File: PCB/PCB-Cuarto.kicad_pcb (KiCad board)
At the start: 4 copper layers, 90 x 100 mm, 80 parts, among them IC100 AP63203WU-7, J100 2604-3102, J200 2171790001, J201 2086-1104, J300 2086-1102, J301 jumper, J302 2086-1104, J303 2086-1104, Q100 CSD19537Q3, Q101 BSS138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

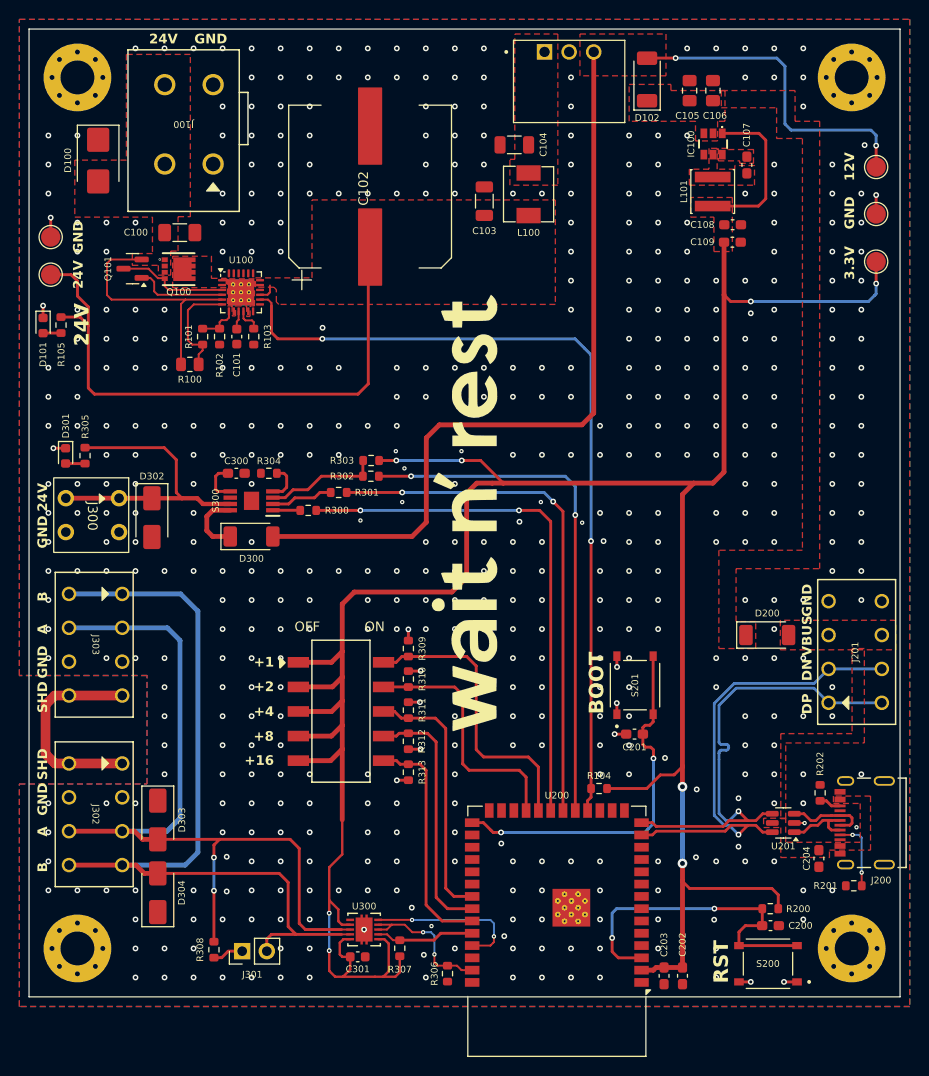
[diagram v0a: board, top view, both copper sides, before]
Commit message: Mejora en ruteo
- Se ha mejorado el ruteo de potencia
- Se ha generado los files para JLCPCB
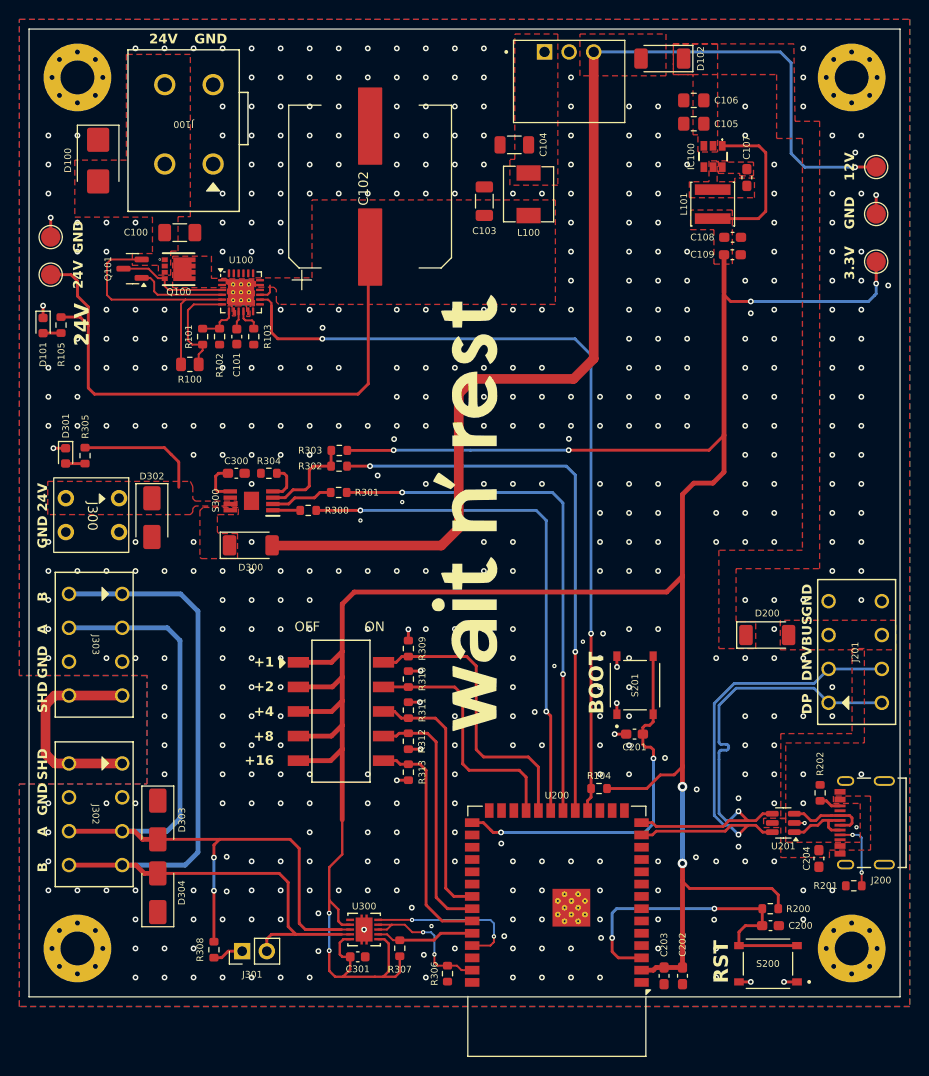
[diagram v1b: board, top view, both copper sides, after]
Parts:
- moved R302 3.45 mm to (137.0, 93.2)
- moved R303 3.45 mm to (137.1, 91.5)
- moved C105 3.45 mm to (173.7, 57.8), turned to 180 degrees
- moved D102 2.67 mm to (170.4, 51.1), turned to 180 degrees
- moved C106 2.22 mm to (173.7, 55.4), turned to 180 degrees
- moved C108 1.30 mm to (177.7, 69.5)
- moved C109 1.30 mm to (177.7, 71.3)
- moved L101 1.30 mm to (175.6, 66.1)
- moved C107 1.30 mm to (179.2, 63.3)
- moved IC100 1.30 mm to (175.7, 61.2)
- moved D300 0.92 mm to (127.9, 101.3)
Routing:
- net Net-(D302-A1): track 31.4 -> 12.9 mm
- net +3.3V: track 287.2 -> 301.4 mm
- net Net-(D300-K): track 6.83 -> 0.00 mm
- net +12V: track 114.6 -> 120.7 mm, vias 2 -> 1
- net /MCU/DOOR_FAULT: track 54.2 -> 58.6 mm
- net Net-(S300-~{FAULT}): track 11.9 -> 9.97 mm
- net /MCU/DOOR_DIAG_EN: track 54.1 -> 54.6 mm
- net GND: vias 520 -> 489
- added copper zone on F.Cu, net Net-(D300-K)
- added copper zone on F.Cu, net Net-(D302-A1)

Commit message: Cambio de footprint del eFuse
- Se cambio el footprint del eFuse debido a que el actual no hay stock en JLCPCB
- Se creo de nuevo los archivos de configuracion de JLCPCB
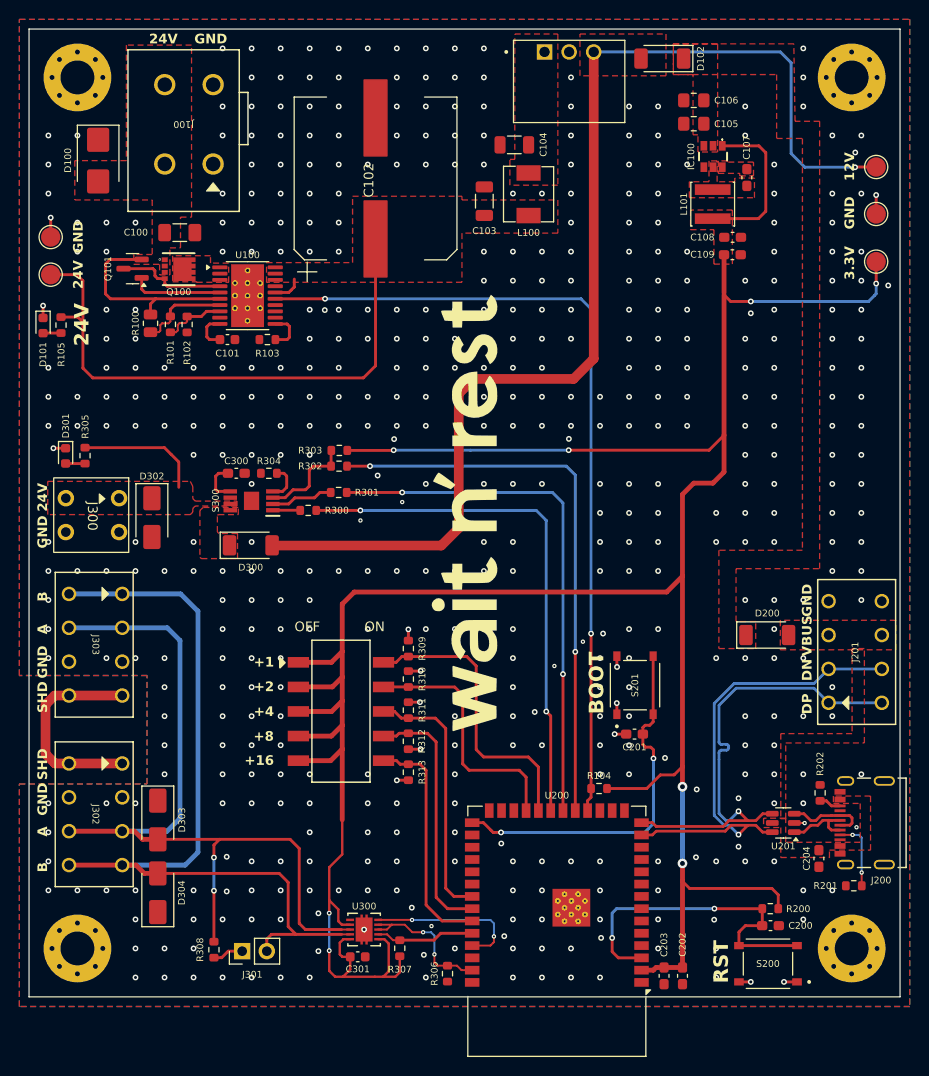
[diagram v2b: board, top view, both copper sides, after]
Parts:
- U100: value TPS26631RGE -> TPS26631PWP; footprint Package_DFN_QFN:Texas_RGE0024H_VQFN-24-1EP_4x4mm_P0.5mm_EP2.7x2.7mm_ThermalVias -> Package_SO:HTSSOP-20-1EP_4.4x6.5mm_P0.65mm_EP3.4x6.5mm_Mask2.96x2.96mm_ThermalVias
- moved R100 5.87 mm to (117.6, 78.4), turned to -90 degrees
- moved R102 3.58 mm to (121.3, 78.5)
- moved R101 3.56 mm to (119.6, 78.5), turned to -90 degrees
- moved R103 1.44 mm to (129.6, 80.1), turned to 180 degrees
- moved C101 1.01 mm to (125.5, 80.1), turned to 180 degrees
- moved C102 1.01 mm to (140.6, 63.6)
- moved U100 0.76 mm to (127.6, 75.5)
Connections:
- U100 pad 10: Net-(U100-ILIM) -> Net-(U100-dVdT)
- U100 pad 11: GND -> Net-(U100-ILIM)
- U100 pad 12: unconnected-(U100-~{SHDN}-Pad12) -> GND
- U100 pad 14: /MCU/FLT -> unconnected-(U100-IMON-Pad14)
- U100 pad 15: +24V -> /MCU/FLT
- U100 pad 16: unconnected-(U100-PGOOD-Pad16) -> +24V
- U100 pad 17: +24V -> unconnected-(U100-PGOOD-Pad17)
- U100 pad 19: unconnected-(U100-NC-Pad19) -> +24V
- U100 pad 20: unconnected-(U100-NC-Pad20) -> +24V
- U100 pad 21: unconnected-(U100-NC-Pad21) -> GND
- U100 pad 3: Net-(Q100-G) -> Net-(Q100-D)
- U100 pad 4: Net-(Q101-G) -> Net-(Q100-G)
- U100 pad 5: /POWER/INPUT -> Net-(Q101-G)
- U100 pad 6: Net-(U100-UVLO) -> /POWER/INPUT
- U100 pad 7: Net-(U100-OVP) -> Net-(U100-UVLO)
- U100 pad 8: GND -> Net-(U100-OVP)
- U100 pad 9: Net-(U100-dVdT) -> GND
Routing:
- net /POWER/INPUT: track 26.0 -> 20.9 mm
- net Net-(U100-OVP): track 4.24 -> 6.64 mm
- net Net-(U100-dVdT): track 1.92 -> 3.99 mm
- net Net-(U100-ILIM): track 2.63 -> 4.25 mm
- net Net-(U100-UVLO): track 10.8 -> 9.40 mm
- net +24V: track 63.1 -> 62.4 mm
- net /MCU/FLT: track 85.6 -> 85.1 mm
- net GND: vias 489 -> 509
